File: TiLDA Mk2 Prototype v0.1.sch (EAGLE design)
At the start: 196 parts, among them IC1 ATSAM3X8EA-AU, IC2 MPU-6050, IC3 LTC4160, IC4 S25FL216K0PMFI011, IC5 AT45DB161E-SSHFHA (NP), IC6 HMC5883LSMD (NP), J10 53261-02, J2 EPD-62684, Q1 DMG2301U, Q10 2N7002KW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

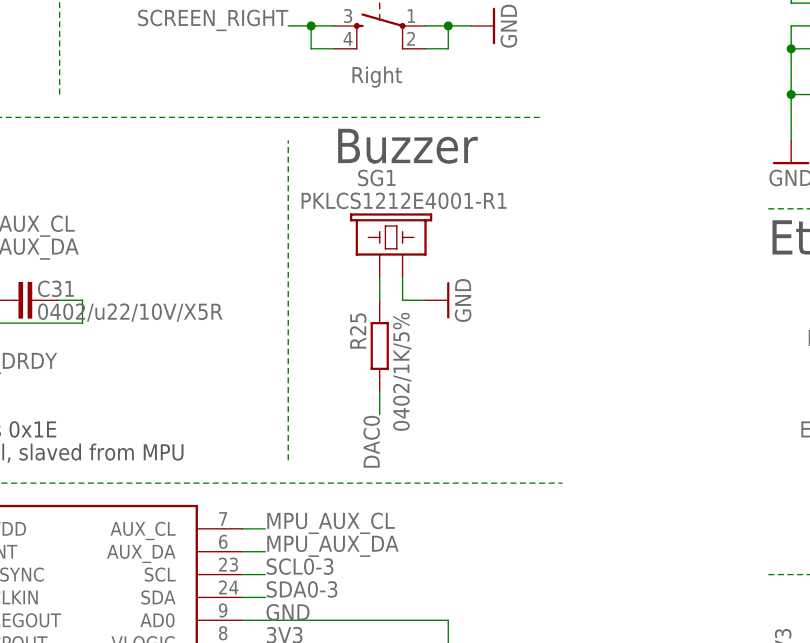
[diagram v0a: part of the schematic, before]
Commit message: Prototype Buzzer disconnect jumper
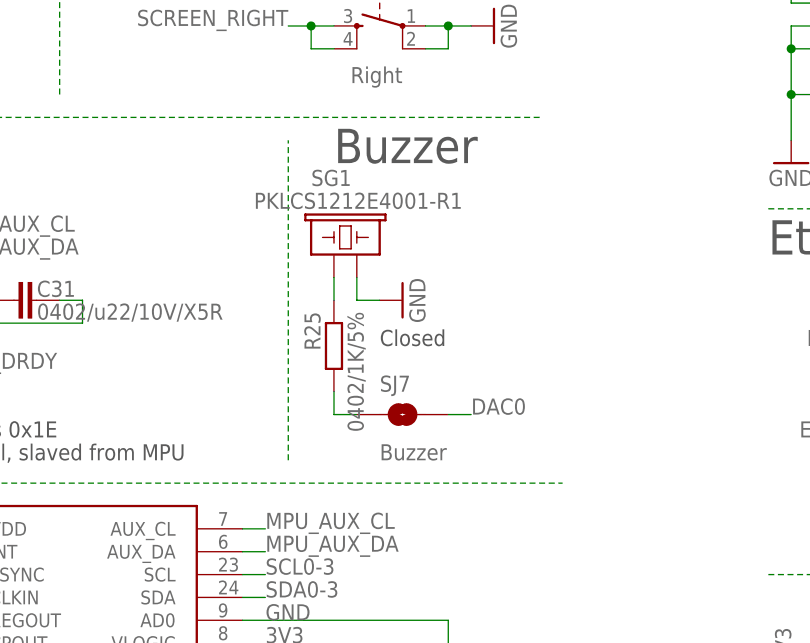
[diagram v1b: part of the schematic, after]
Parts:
- added SJ7: Buzzer, TiLDA Mk2 Parts:SOLDERJUMPERTRACE
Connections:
- net N$28 renamed BUZZER+
- new net BUZZER_RES: R25.2, SJ7.1
- net DAC0: now also SJ7.2; no longer R25.2
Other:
- moved on the sheet: R25, SG1
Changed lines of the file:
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@@
 <part name="C32" library="TiLDA Mk2 Parts" deviceset="C-EU" device="C0402-ARDUINO-ROUND" value="0402/100n/10V/Y5V"/>
 <part name="GND56" library="TiLDA Mk2 Parts" deviceset="GND" device=""/>
+<part name="SJ7" library="TiLDA Mk2 Parts" deviceset="SOLDERJUMPER" device="TRACE" value="Buzzer"/>
 </parts>
 <sheets>
@@
 <text x="175.26" y="7.62" size="1.778" layer="97">Supports 512B Page erase</text>
 <text x="175.26" y="5.08" size="1.778" layer="97">But more expensive</text>
+<text x="363.22" y="71.12" size="1.778" layer="97">Closed</text>
 </plain>
 <instances>
@@
 </instance>
 <instance part="JP8" gate="G$1" x="15.24" y="185.42"/>
-<instance part="SG1" gate="G$1" x="363.22" y="81.28" smashed="yes">
-<attribute name="NAME" x="360.68" y="88.9" size="1.778" layer="95"/>
-<attribute name="VALUE" x="354.33" y="86.36" size="1.778" layer="96"/>
+<instance part="SG1" gate="G$1" x="358.14" y="81.28" smashed="yes">
+<attribute name="NAME" x="355.6" y="88.9" size="1.778" layer="95"/>
+<attribute name="VALUE" x="349.25" y="86.36" size="1.778" layer="96"/>
 </instance>
 <instance part="C1" gate="G$1" x="96.52" y="236.22" smashed="yes">
@@
 <attribute name="VALUE" x="727.202" y="224.79" size="1.778" layer="96" rot="R90"/>
 </instance>
-<instance part="GND53" gate="1" x="370.84" y="76.2" rot="R90"/>
-<instance part="R25" gate="G$1" x="363.22" y="71.12" rot="MR270"/>
+<instance part="GND53" gate="1" x="365.76" y="76.2" rot="R90"/>
+<instance part="R25" gate="G$1" x="358.14" y="71.12" rot="MR270"/>
 <instance part="IC3" gate="G$1" x="60.96" y="60.96"/>
 <instance part="L2" gate="G$1" x="93.98" y="73.66" rot="MR90"/>
@@
 </instance>
 <instance part="GND56" gate="1" x="119.38" y="5.08"/>
+<instance part="SJ7" gate="1" x="365.76" y="63.5"/>
 </instances>
 <busses>
@@
 <segment>
 <pinref part="SG1" gate="G$1" pin="2"/>
-<wire x1="365.76" y1="76.2" x2="365.76" y2="78.74" width="0.1524" layer="91"/>
+<wire x1="360.68" y1="76.2" x2="360.68" y2="78.74" width="0.1524" layer="91"/>
 <pinref part="GND53" gate="1" pin="GND"/>
-<wire x1="368.3" y1="76.2" x2="365.76" y2="76.2" width="0.1524" layer="91"/>
+<wire x1="363.22" y1="76.2" x2="360.68" y2="76.2" width="0.1524" layer="91"/>
 </segment>
 <segment>
@@
 </segment>
 <segment>
-<pinref part="R25" gate="G$1" pin="2"/>
-<wire x1="363.22" y1="63.5" x2="363.22" y2="66.04" width="0.1524" layer="91"/>
-<label x="363.22" y="63.5" size="1.778" layer="95" rot="MR270"/>
+<pinref part="SJ7" gate="1" pin="2"/>
+<wire x1="373.38" y1="63.5" x2="370.84" y2="63.5" width="0.1524" layer="91"/>
+<label x="373.38" y="63.5" size="1.778" layer="95"/>
 </segment>
 </net>
@@
 </segment>
 </net>
-<net name="N$28" class="0">
+<net name="BUZZER+" class="0">
 <segment>
 <pinref part="SG1" gate="G$1" pin="1"/>
-<wire x1="363.22" y1="76.2" x2="363.22" y2="78.74" width="0.1524" layer="91"/>
+<wire x1="358.14" y1="76.2" x2="358.14" y2="78.74" width="0.1524" layer="91"/>
 <pinref part="R25" gate="G$1" pin="1"/>
 </segment>
@@
 </segment>
 </net>
+<net name="BUZZER_RES" class="0">
+<segment>
+<pinref part="R25" gate="G$1" pin="2"/>
+<wire x1="360.68" y1="63.5" x2="358.14" y2="63.5" width="0.1524" layer="91"/>
+<wire x1="358.14" y1="63.5" x2="358.14" y2="66.04" width="0.1524" layer="91"/>
+<pinref part="SJ7" gate="1" pin="1"/>
+</segment>
+</net>

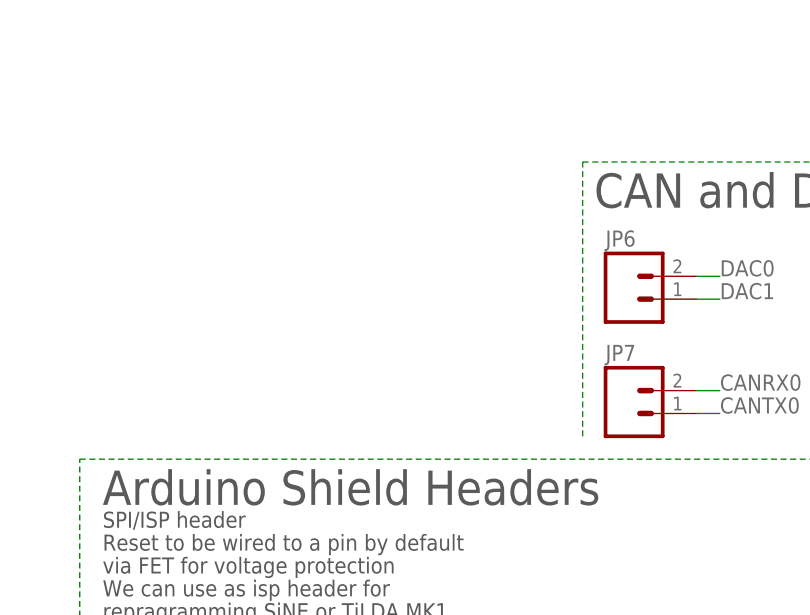
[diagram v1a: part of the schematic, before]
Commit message: Prototype: Adding I2C pull-up’s
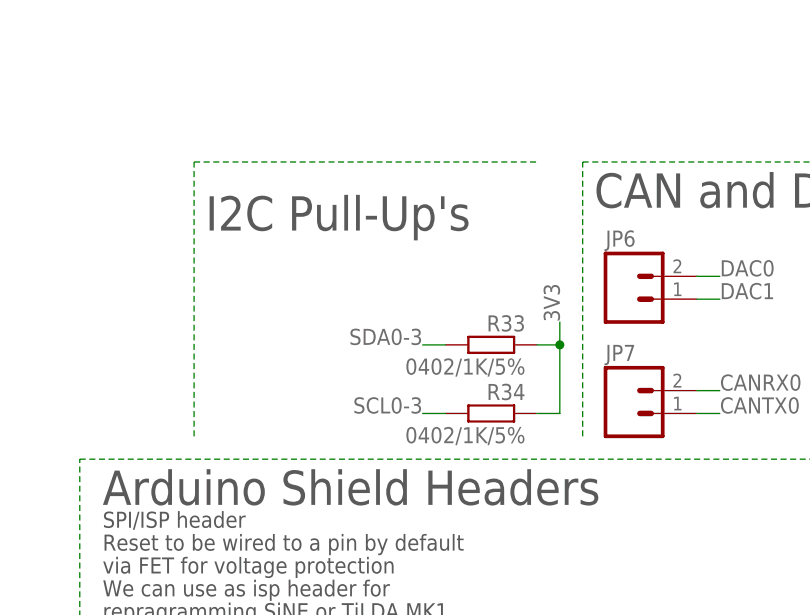
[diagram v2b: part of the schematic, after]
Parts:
- added R33, R34: 0402/1K/5%, TiLDA Mk2 Parts:R-EU_R0402-ARDUINO-ROUND
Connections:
- net 3V3: now also R33.1, R34.1
- net SCL0-3: now also R34.2
- net SDA0-3: now also R33.2
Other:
- note added: "I2C Pull-Up's"

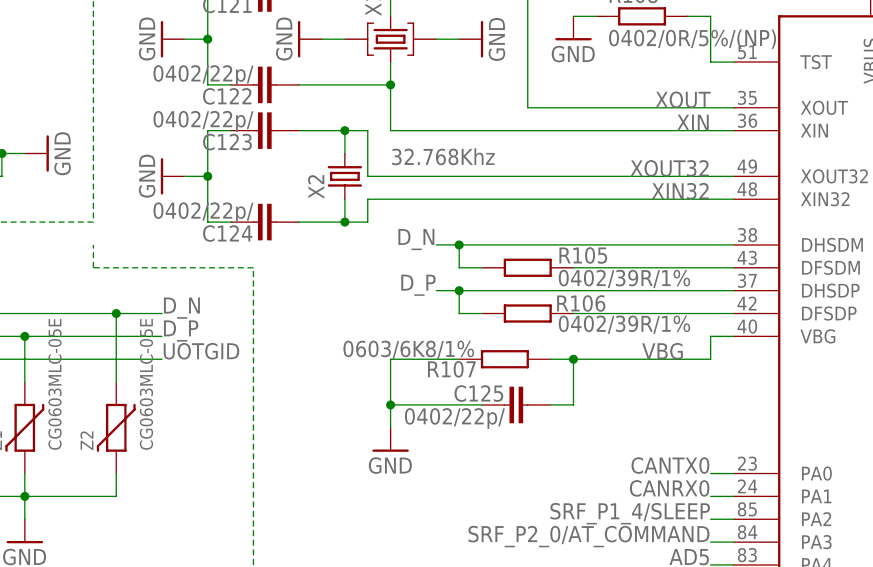
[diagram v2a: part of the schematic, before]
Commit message: Prototype: Reworked USB Traces, tweaked some other bits
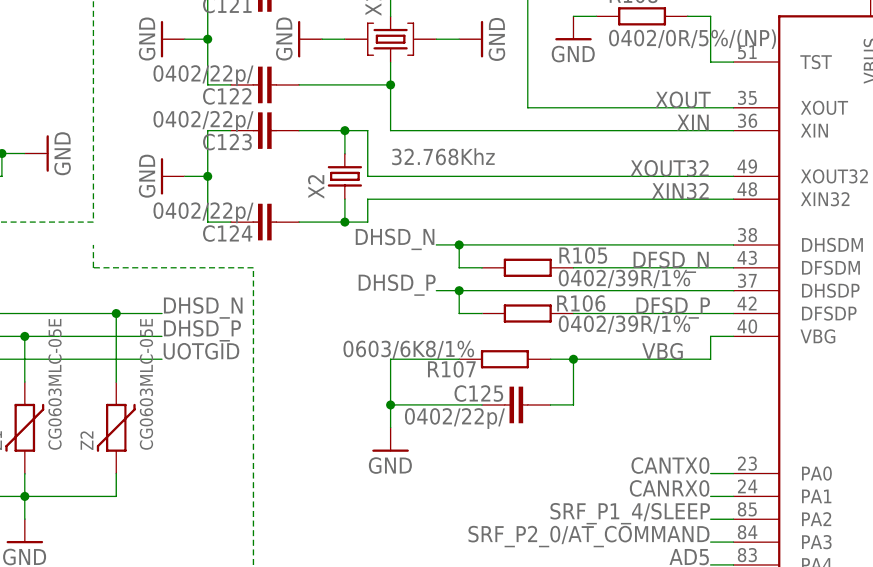
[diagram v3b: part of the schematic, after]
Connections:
- net D_N renamed DHSD_N
- net D_P renamed DHSD_P
- net N$31 renamed DFSD_P
- net N$33 renamed DFSD_N
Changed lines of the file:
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@@
 </segment>
 </net>
-<net name="N$31" class="0">
+<net name="DFSD_P" class="1">
 <segment>
 <pinref part="IC1" gate="G$1" pin="DFSDP"/>
 <pinref part="R106" gate="G$1" pin="2"/>
 <wire x1="515.62" y1="167.64" x2="497.84" y2="167.64" width="0.1524" layer="91"/>
+<label x="513.08" y="167.64" size="1.778" layer="95" rot="MR0"/>
 </segment>
 </net>
-<net name="D_P" class="1">
+<net name="DHSD_P" class="1">
 <segment>
 <pinref part="IC1" gate="G$1" pin="DHSDP"/>
@@
 </segment>
 </net>
-<net name="N$33" class="0">
+<net name="DFSD_N" class="1">
 <segment>
 <pinref part="IC1" gate="G$1" pin="DFSDM"/>
 <pinref part="R105" gate="G$1" pin="2"/>
 <wire x1="515.62" y1="172.72" x2="497.84" y2="172.72" width="0.1524" layer="91"/>
+<label x="513.08" y="172.72" size="1.778" layer="95" rot="MR0"/>
 </segment>
 </net>
-<net name="D_N" class="1">
+<net name="DHSD_N" class="1">
 <segment>
 <pinref part="IC1" gate="G$1" pin="DHSDM"/>

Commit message: Prototype: Updating IMU Footprints,
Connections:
- net 3V3: no longer C27.2, C4.1, C8.2, IC2.VDD, IC2.VLOGIC, IC6.S1, IC6.VDD, IC6.VDDIO
- net VBACKUP: now also C27.2, C4.1, C8.2, IC2.VDD, IC2.VLOGIC, IC6.S1, IC6.VDD, IC6.VDDIO
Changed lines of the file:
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@@
-</segment>
-<segment>
-<label x="309.88" y="50.8" size="1.778" layer="95" rot="MR0"/>
-<pinref part="C4" gate="G$1" pin="1"/>
-<wire x1="312.42" y1="50.8" x2="266.7" y2="50.8" width="0.1524" layer="91"/>
-<pinref part="IC2" gate="G$1" pin="VDD"/>
 </segment>
 <segment>
@@
 </segment>
 <segment>
-<wire x1="347.98" y1="38.1" x2="350.52" y2="38.1" width="0.1524" layer="91"/>
-<label x="350.52" y="38.1" size="1.778" layer="95"/>
-<pinref part="IC2" gate="G$1" pin="VLOGIC"/>
-<pinref part="C8" gate="G$1" pin="2"/>
-<wire x1="350.52" y1="38.1" x2="350.52" y2="33.02" width="0.1524" layer="91"/>
-<wire x1="350.52" y1="33.02" x2="353.06" y2="33.02" width="0.1524" layer="91"/>
-</segment>
-<segment>
 <pinref part="R4" gate="G$1" pin="2"/>
 <wire x1="276.86" y1="15.24" x2="279.4" y2="15.24" width="0.1524" layer="91"/>
@@
 <wire x1="58.42" y1="157.48" x2="58.42" y2="165.1" width="0.1524" layer="91"/>
 <junction x="58.42" y="157.48"/>
-</segment>
-<segment>
-<pinref part="IC6" gate="G$1" pin="S1"/>
-<wire x1="284.48" y1="78.74" x2="287.02" y2="78.74" width="0.1524" layer="91"/>
-<pinref part="IC6" gate="G$1" pin="VDD"/>
-<wire x1="284.48" y1="83.82" x2="287.02" y2="83.82" width="0.1524" layer="91"/>
-<pinref part="IC6" gate="G$1" pin="VDDIO"/>
-<wire x1="284.48" y1="81.28" x2="287.02" y2="81.28" width="0.1524" layer="91"/>
-<wire x1="284.48" y1="83.82" x2="284.48" y2="81.28" width="0.1524" layer="91"/>
-<wire x1="284.48" y1="78.74" x2="284.48" y2="81.28" width="0.1524" layer="91"/>
-<junction x="284.48" y="81.28"/>
-<junction x="284.48" y="83.82"/>
-<label x="276.86" y="83.82" size="1.778" layer="95" rot="MR0"/>
-<wire x1="284.48" y1="83.82" x2="281.94" y2="83.82" width="0.1524" layer="91"/>
-<pinref part="C27" gate="G$1" pin="2"/>
-<wire x1="276.86" y1="83.82" x2="281.94" y2="83.82" width="0.1524" layer="91"/>
-<wire x1="281.94" y1="83.82" x2="281.94" y2="78.74" width="0.1524" layer="91"/>
-<junction x="281.94" y="83.82"/>
 </segment>
 <segment>
@@
 <wire x1="581.66" y1="228.6" x2="581.66" y2="205.74" width="0.1524" layer="91"/>
 </segment>
-</net>
+<segment>
+<label x="309.88" y="50.8" size="1.778" layer="95" rot="MR0"/>
+<pinref part="C4" gate="G$1" pin="1"/>
+<wire x1="312.42" y1="50.8" x2="266.7" y2="50.8" width="0.1524" layer="91"/>
+<pinref part="IC2" gate="G$1" pin="VDD"/>
+</segment>
+<segment>
+<wire x1="347.98" y1="38.1" x2="350.52" y2="38.1" width="0.1524" layer="91"/>
+<label x="350.52" y="38.1" size="1.778" layer="95"/>
+<pinref part="IC2" gate="G$1" pin="VLOGIC"/>
+<pinref part="C8" gate="G$1" pin="2"/>
+<wire x1="350.52" y1="38.1" x2="350.52" y2="33.02" width="0.1524" layer="91"/>
+<wire x1="350.52" y1="33.02" x2="353.06" y2="33.02" width="0.1524" layer="91"/>
+</segment>
+<segment>
+<pinref part="IC6" gate="G$1" pin="S1"/>
+<wire x1="284.48" y1="78.74" x2="287.02" y2="78.74" width="0.1524" layer="91"/>
+<pinref part="IC6" gate="G$1" pin="VDD"/>
+<wire x1="284.48" y1="83.82" x2="287.02" y2="83.82" width="0.1524" layer="91"/>
+<pinref part="IC6" gate="G$1" pin="VDDIO"/>
+<wire x1="284.48" y1="81.28" x2="287.02" y2="81.28" width="0.1524" layer="91"/>
+<wire x1="284.48" y1="83.82" x2="284.48" y2="81.28" width="0.1524" layer="91"/>
+<wire x1="284.48" y1="78.74" x2="284.48" y2="81.28" width="0.1524" layer="91"/>
+<junction x="284.48" y="81.28"/>
+<junction x="284.48" y="83.82"/>
+<label x="276.86" y="83.82" size="1.778" layer="95" rot="MR0"/>
+<wire x1="284.48" y1="83.82" x2="281.94" y2="83.82" width="0.1524" layer="91"/>
+<pinref part="C27" gate="G$1" pin="2"/>
+<wire x1="276.86" y1="83.82" x2="281.94" y2="83.82" width="0.1524" layer="91"/>
+<wire x1="281.94" y1="83.82" x2="281.94" y2="78.74" width="0.1524" layer="91"/>
+<junction x="281.94" y="83.82"/>
+</segment>
+</net>

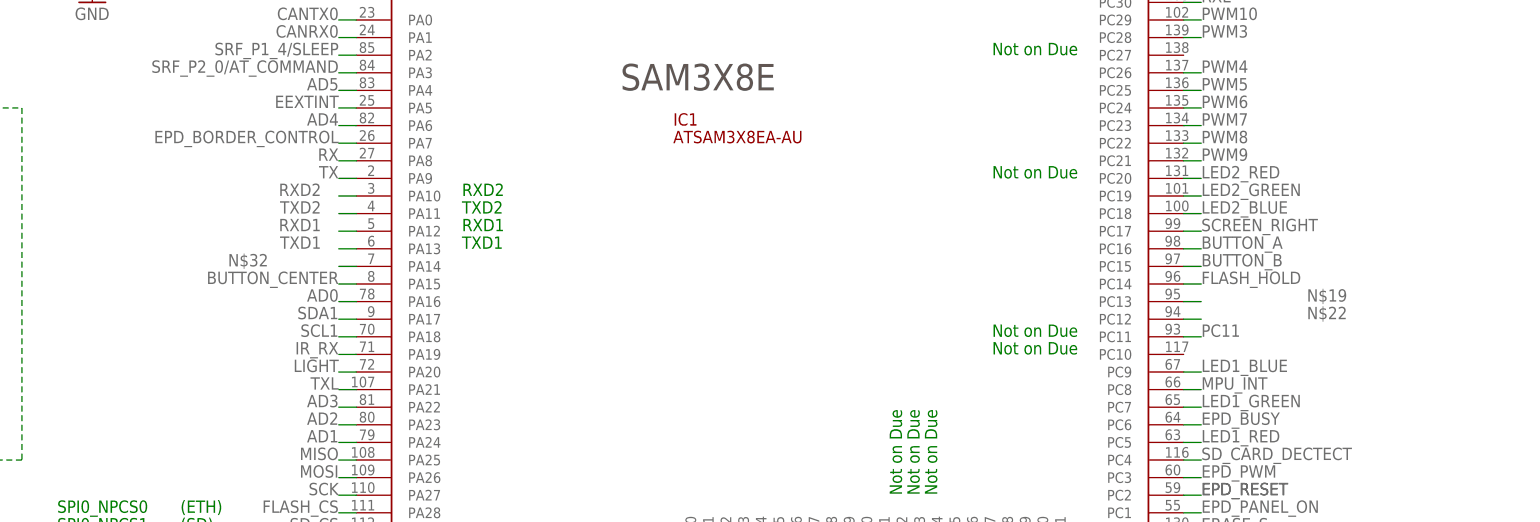
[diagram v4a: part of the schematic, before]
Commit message: Prototype: Swapping MPU_INT onto a wake up pin
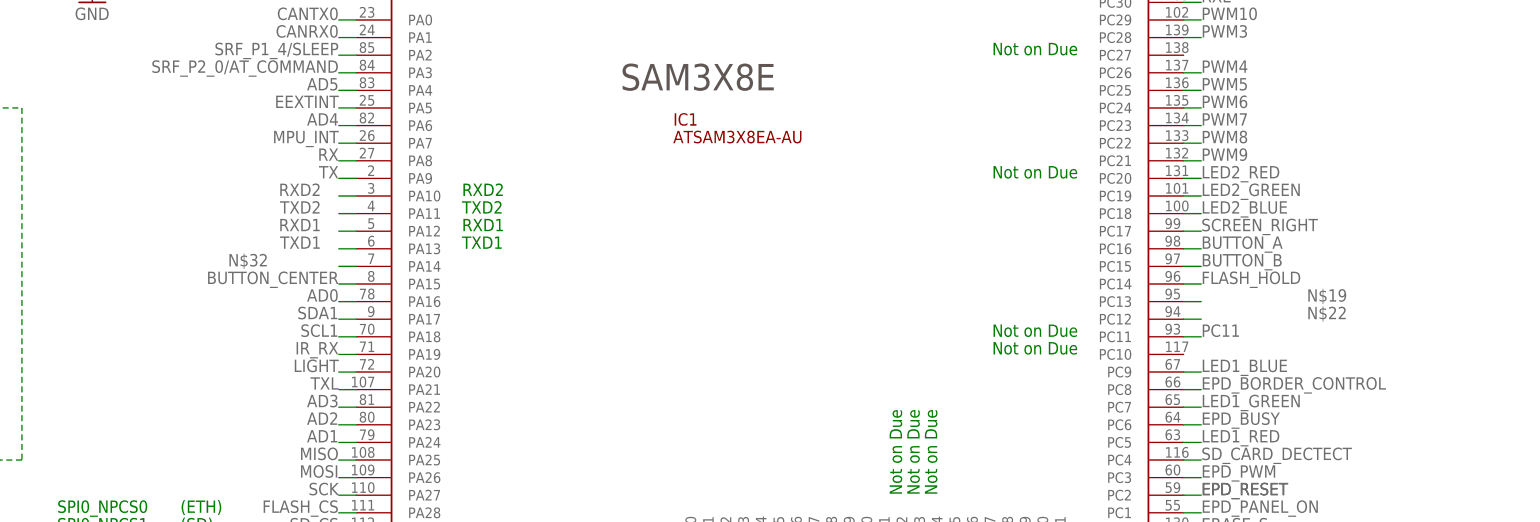
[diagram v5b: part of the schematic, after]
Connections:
- net EPD_BORDER_CONTROL: now also IC1.PC8; no longer IC1.PA7
- net MPU_INT: now also IC1.PA7; no longer IC1.PC8
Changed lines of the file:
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@@
 </segment>
 <segment>
-<pinref part="IC1" gate="G$1" pin="PA7"/>
-<wire x1="513.08" y1="132.08" x2="515.62" y2="132.08" width="0.1524" layer="91"/>
-<label x="513.08" y="132.08" size="1.778" layer="95" rot="MR0"/>
+<pinref part="IC1" gate="G$1" pin="PC8"/>
+<wire x1="637.54" y1="96.52" x2="635" y2="96.52" width="0.1524" layer="91"/>
+<label x="637.54" y="96.52" size="1.778" layer="95"/>
 </segment>
 </net>
@@
 </segment>
 <segment>
-<pinref part="IC1" gate="G$1" pin="PC8"/>
-<wire x1="637.54" y1="96.52" x2="635" y2="96.52" width="0.1524" layer="91"/>
-<label x="637.54" y="96.52" size="1.778" layer="95"/>
-</segment>
-</net>
+<pinref part="IC1" gate="G$1" pin="PA7"/>
+<wire x1="513.08" y1="132.08" x2="515.62" y2="132.08" width="0.1524" layer="91"/>
+<label x="513.08" y="132.08" size="1.778" layer="95" rot="MR0"/>
+</segment>
+</net>
